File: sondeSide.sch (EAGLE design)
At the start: 33 parts

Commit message: I think its done, just needs labels
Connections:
- net 3.3V: now also JP15.1
- net 5V: no longer U$1.UGND1, U$1.UGND2
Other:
- moved on the sheet: JP25
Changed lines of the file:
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@@
 <sheet>
 <plain>
-<text x="-17.78" y="50.8" size="1.778" layer="91">Teensy VIN is on other side</text>
+<text x="12.7" y="50.8" size="1.778" layer="91">Teensy VIN is on other side</text>
 </plain>
 <instances>
@@
 <instance part="JP23" gate="G$1" x="-60.96" y="0" rot="R180"/>
 <instance part="JP24" gate="G$1" x="-60.96" y="-2.54" rot="R180"/>
-<instance part="JP25" gate="G$1" x="-5.08" y="55.88"/>
-<instance part="U$1" gate="G$1" x="-10.16" y="25.4"/>
+<instance part="JP25" gate="G$1" x="25.4" y="55.88"/>
+<instance part="U$1" gate="G$1" x="-10.16" y="43.18"/>
 </instances>
 <busses>
@@
 <wire x1="66.04" y1="12.7" x2="60.96" y2="12.7" width="0.1524" layer="91"/>
 <label x="60.96" y="12.7" size="1.778" layer="95" rot="R180"/>
+</segment>
+<segment>
+<pinref part="JP15" gate="G$1" pin="1"/>
+<wire x1="-58.42" y1="20.32" x2="-33.02" y2="20.32" width="0.1524" layer="91"/>
+<label x="-38.1" y="20.32" size="1.778" layer="95" rot="R180"/>
 </segment>
 </net>
@@
 <segment>
 <pinref part="JP25" gate="G$1" pin="1"/>
-<wire x1="-7.62" y1="55.88" x2="-12.7" y2="55.88" width="0.1524" layer="91"/>
-<label x="-15.24" y="55.88" size="1.778" layer="95" rot="R180"/>
-<pinref part="U$1" gate="G$1" pin="UGND1"/>
-<pinref part="U$1" gate="G$1" pin="UGND2"/>
-<wire x1="-12.7" y1="55.88" x2="-15.24" y2="55.88" width="0.1524" layer="91"/>
-<junction x="-12.7" y="55.88"/>
-</segment>
-</net>
+<wire x1="22.86" y1="55.88" x2="15.24" y2="55.88" width="0.1524" layer="91"/>
+<label x="15.24" y="55.88" size="1.778" layer="95" rot="R180"/>
+</segment>
+</net>

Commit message: I think its done
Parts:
- renumbered JP25 to VIN
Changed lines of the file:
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@@
 <part name="JP23" library="pinhead" library_urn="urn:adsk.eagle:library:325" deviceset="PINHD-1X1" device="" package3d_urn="urn:adsk.eagle:package:22485/2"/>
 <part name="JP24" library="pinhead" library_urn="urn:adsk.eagle:library:325" deviceset="PINHD-1X1" device="" package3d_urn="urn:adsk.eagle:package:22485/2"/>
-<part name="JP25" library="pinhead" library_urn="urn:adsk.eagle:library:325" deviceset="PINHD-1X1" device="" package3d_urn="urn:adsk.eagle:package:22485/2"/>
+<part name="VIN" library="pinhead" library_urn="urn:adsk.eagle:library:325" deviceset="PINHD-1X1" device="" package3d_urn="urn:adsk.eagle:package:22485/2"/>
 <part name="U$1" library="Teensy356" deviceset="TEENSY_3.5/3.6" device=""/>
 </parts>
@@
 <instance part="JP23" gate="G$1" x="-60.96" y="0" rot="R180"/>
 <instance part="JP24" gate="G$1" x="-60.96" y="-2.54" rot="R180"/>
-<instance part="JP25" gate="G$1" x="25.4" y="55.88"/>
+<instance part="VIN" gate="G$1" x="25.4" y="55.88"/>
 <instance part="U$1" gate="G$1" x="-10.16" y="43.18"/>
 </instances>
@@
 </segment>
 <segment>
-<pinref part="JP25" gate="G$1" pin="1"/>
+<pinref part="VIN" gate="G$1" pin="1"/>
 <wire x1="22.86" y1="55.88" x2="15.24" y2="55.88" width="0.1524" layer="91"/>
 <label x="15.24" y="55.88" size="1.778" layer="95" rot="R180"/>

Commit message: Without external 3.3v step down
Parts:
- removed U$1: TEENSY_3.5/3.6, Teensy356:TEENSY_3.5/3.6
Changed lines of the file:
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@@
 <part name="JP24" library="pinhead" library_urn="urn:adsk.eagle:library:325" deviceset="PINHD-1X1" device="" package3d_urn="urn:adsk.eagle:package:22485/2"/>
 <part name="VIN" library="pinhead" library_urn="urn:adsk.eagle:library:325" deviceset="PINHD-1X1" device="" package3d_urn="urn:adsk.eagle:package:22485/2"/>
-<part name="U$1" library="Teensy356" deviceset="TEENSY_3.5/3.6" device=""/>
 </parts>
 <sheets>
@@
 <instance part="JP24" gate="G$1" x="-60.96" y="-2.54" rot="R180"/>
 <instance part="VIN" gate="G$1" x="25.4" y="55.88"/>
-<instance part="U$1" gate="G$1" x="-10.16" y="43.18"/>
 </instances>
 <busses>
@@
 </drawing>
 <compatibility>
-<note version="6.3" minversion="6.2.2" severity="warning">
-Since Version 6.2.2 text objects can contain more than one line,
-which will not be processed correctly with this version.
-</note>
 <note version="8.2" severity="warning">
 Since Version 8.2, EAGLE supports online libraries. The ids

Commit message: Pre-routing
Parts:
- removed VIN: (no value), pinhead:PINHD-1X1
- added STEP-DOWN: 22-23-2041, con-molex:22-23-2041
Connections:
- net 3.3V: now also STEP-DOWN-1.S
- net 5V: now also STEP-DOWN-3.S; no longer VIN.1
- net GND: now also STEP-DOWN-2.S
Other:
- note removed: "Teensy VIN is on other side"
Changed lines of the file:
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@@
 <part name="JP23" library="pinhead" library_urn="urn:adsk.eagle:library:325" deviceset="PINHD-1X1" device="" package3d_urn="urn:adsk.eagle:package:22485/2"/>
 <part name="JP24" library="pinhead" library_urn="urn:adsk.eagle:library:325" deviceset="PINHD-1X1" device="" package3d_urn="urn:adsk.eagle:package:22485/2"/>
-<part name="VIN" library="pinhead" library_urn="urn:adsk.eagle:library:325" deviceset="PINHD-1X1" device="" package3d_urn="urn:adsk.eagle:package:22485/2"/>
+<part name="STEP-DOWN" library="con-molex" library_urn="urn:adsk.eagle:library:165" deviceset="22-23-2041" device=""/>
 </parts>
 <sheets>
 <sheet>
 <plain>
-<text x="12.7" y="50.8" size="1.778" layer="91">Teensy VIN is on other side</text>
 </plain>
 <instances>
@@
 <instance part="JP23" gate="G$1" x="-60.96" y="0" rot="R180"/>
 <instance part="JP24" gate="G$1" x="-60.96" y="-2.54" rot="R180"/>
-<instance part="VIN" gate="G$1" x="25.4" y="55.88"/>
+<instance part="STEP-DOWN" gate="-1" x="68.58" y="53.34"/>
+<instance part="STEP-DOWN" gate="-2" x="68.58" y="50.8"/>
+<instance part="STEP-DOWN" gate="-3" x="68.58" y="48.26"/>
+<instance part="STEP-DOWN" gate="-4" x="68.58" y="45.72"/>
 </instances>
 <busses>
@@
 <wire x1="-58.42" y1="20.32" x2="-33.02" y2="20.32" width="0.1524" layer="91"/>
 <label x="-38.1" y="20.32" size="1.778" layer="95" rot="R180"/>
+</segment>
+<segment>
+<pinref part="STEP-DOWN" gate="-1" pin="S"/>
+<wire x1="66.04" y1="53.34" x2="60.96" y2="53.34" width="0.1524" layer="91"/>
+<label x="60.96" y="53.34" size="1.778" layer="95" rot="R180"/>
 </segment>
 </net>
@@
 <wire x1="60.96" y1="5.08" x2="66.04" y2="5.08" width="0.1524" layer="91"/>
 <label x="60.96" y="5.08" size="1.778" layer="95" rot="R180"/>
+</segment>
+<segment>
+<pinref part="STEP-DOWN" gate="-2" pin="S"/>
+<wire x1="60.96" y1="50.8" x2="66.04" y2="50.8" width="0.1524" layer="91"/>
+<label x="60.96" y="50.8" size="1.778" layer="95" rot="R180"/>
 </segment>
 </net>
@@
 </segment>
 <segment>
-<pinref part="VIN" gate="G$1" pin="1"/>
-<wire x1="22.86" y1="55.88" x2="15.24" y2="55.88" width="0.1524" layer="91"/>
-<label x="15.24" y="55.88" size="1.778" layer="95" rot="R180"/>
-</segment>
-</net>
+<pinref part="STEP-DOWN" gate="-3" pin="S"/>
+<wire x1="66.04" y1="48.26" x2="60.96" y2="48.26" width="0.1524" layer="91"/>
+<label x="60.96" y="48.26" size="1.778" layer="95" rot="R180"/>
+</segment>
+</net>

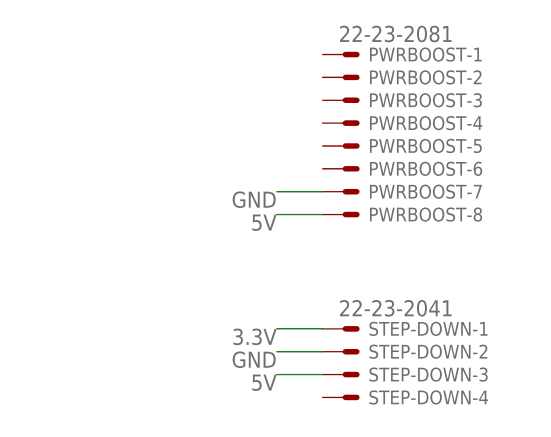
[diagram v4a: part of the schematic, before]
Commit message: Everything but ground plane
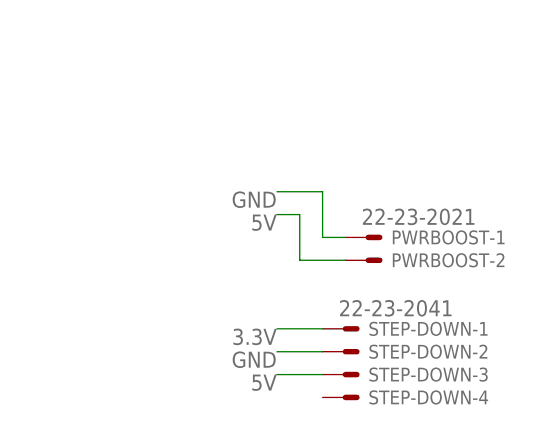
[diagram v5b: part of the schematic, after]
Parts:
- PWRBOOST: value 22-23-2081 -> 22-23-2021; device con-molex:22-23-2081 -> con-molex:22-23-2021; SPICEPREFIX X -> (none)
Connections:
- net 5V: now also PWRBOOST-2.S; no longer PWRBOOST-8.S
- net GND: now also PWRBOOST-1.S; no longer PWRBOOST-7.S
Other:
- moved on the sheet: PWRBOOST-1, PWRBOOST-2
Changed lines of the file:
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@@
 <layer number="2" name="Route2" color="1" fill="3" visible="no" active="no"/>
 <layer number="3" name="Route3" color="4" fill="3" visible="no" active="no"/>
+<layer number="4" name="Route4" color="1" fill="4" visible="no" active="no"/>
+<layer number="5" name="Route5" color="4" fill="4" visible="no" active="no"/>
+<layer number="6" name="Route6" color="1" fill="8" visible="no" active="no"/>
+<layer number="7" name="Route7" color="4" fill="8" visible="no" active="no"/>
+<layer number="8" name="Route8" color="1" fill="2" visible="no" active="no"/>
+<layer number="9" name="Route9" color="4" fill="2" visible="no" active="no"/>
+<layer number="10" name="Route10" color="1" fill="7" visible="no" active="no"/>
+<layer number="11" name="Route11" color="4" fill="7" visible="no" active="no"/>
+<layer number="12" name="Route12" color="1" fill="5" visible="no" active="no"/>
+<layer number="13" name="Route13" color="4" fill="5" visible="no" active="no"/>
 <layer number="14" name="Route14" color="1" fill="6" visible="no" active="no"/>
 <layer number="15" name="Route15" color="4" fill="6" visible="no" active="no"/>
@@
 </classes>
 <parts>
-<part name="PWRBOOST" library="con-molex" library_urn="urn:adsk.eagle:library:165" deviceset="22-23-2081" device="">
-<attribute name="SPICEPREFIX" value="X"/>
-</part>
 <part name="STEP-UP" library="con-molex" library_urn="urn:adsk.eagle:library:165" deviceset="22-23-2031" device=""/>
 <part name="SONDE" library="con-molex" library_urn="urn:adsk.eagle:library:165" deviceset="22-23-2051" device=""/>
@@
 <part name="JP24" library="pinhead" library_urn="urn:adsk.eagle:library:325" deviceset="PINHD-1X1" device="" package3d_urn="urn:adsk.eagle:package:22485/2"/>
 <part name="STEP-DOWN" library="con-molex" library_urn="urn:adsk.eagle:library:165" deviceset="22-23-2041" device=""/>
+<part name="PWRBOOST" library="con-molex" library_urn="urn:adsk.eagle:library:165" deviceset="22-23-2021" device=""/>
 </parts>
 <sheets>
@@
 </plain>
 <instances>
-<instance part="PWRBOOST" gate="-1" x="68.58" y="83.82"/>
-<instance part="PWRBOOST" gate="-2" x="68.58" y="81.28"/>
-<instance part="PWRBOOST" gate="-3" x="68.58" y="78.74"/>
-<instance part="PWRBOOST" gate="-4" x="68.58" y="76.2"/>
-<instance part="PWRBOOST" gate="-5" x="68.58" y="73.66"/>
-<instance part="PWRBOOST" gate="-6" x="68.58" y="71.12"/>
-<instance part="PWRBOOST" gate="-7" x="68.58" y="68.58"/>
-<instance part="PWRBOOST" gate="-8" x="68.58" y="66.04"/>
 <instance part="STEP-UP" gate="-1" x="68.58" y="30.48"/>
 <instance part="STEP-UP" gate="-2" x="68.58" y="27.94"/>
@@
 <instance part="STEP-DOWN" gate="-3" x="68.58" y="48.26"/>
 <instance part="STEP-DOWN" gate="-4" x="68.58" y="45.72"/>
+<instance part="PWRBOOST" gate="-1" x="71.12" y="63.5"/>
+<instance part="PWRBOOST" gate="-2" x="71.12" y="60.96"/>
 </instances>
 <busses>
@@
 </segment>
 <segment>
-<pinref part="PWRBOOST" gate="-7" pin="S"/>
 <wire x1="66.04" y1="68.58" x2="60.96" y2="68.58" width="0.1524" layer="91"/>
 <label x="60.96" y="68.58" size="1.778" layer="95" rot="R180"/>
+<pinref part="PWRBOOST" gate="-1" pin="S"/>
+<wire x1="68.58" y1="63.5" x2="66.04" y2="63.5" width="0.1524" layer="91"/>
+<wire x1="66.04" y1="63.5" x2="66.04" y2="68.58" width="0.1524" layer="91"/>
 </segment>
 <segment>
@@
 <net name="5V" class="0">
 <segment>
-<pinref part="PWRBOOST" gate="-8" pin="S"/>
-<wire x1="60.96" y1="66.04" x2="66.04" y2="66.04" width="0.1524" layer="91"/>
+<wire x1="60.96" y1="66.04" x2="63.5" y2="66.04" width="0.1524" layer="91"/>
 <label x="60.96" y="66.04" size="1.778" layer="95" rot="R180"/>
-</segment>
-<segment>
+<pinref part="PWRBOOST" gate="-2" pin="S"/>
+<wire x1="63.5" y1="66.04" x2="63.5" y2="60.96" width="0.1524" layer="91"/>
+<wire x1="63.5" y1="60.96" x2="68.58" y2="60.96" width="0.1524" layer="91"/>
+</segment>
+<segment>

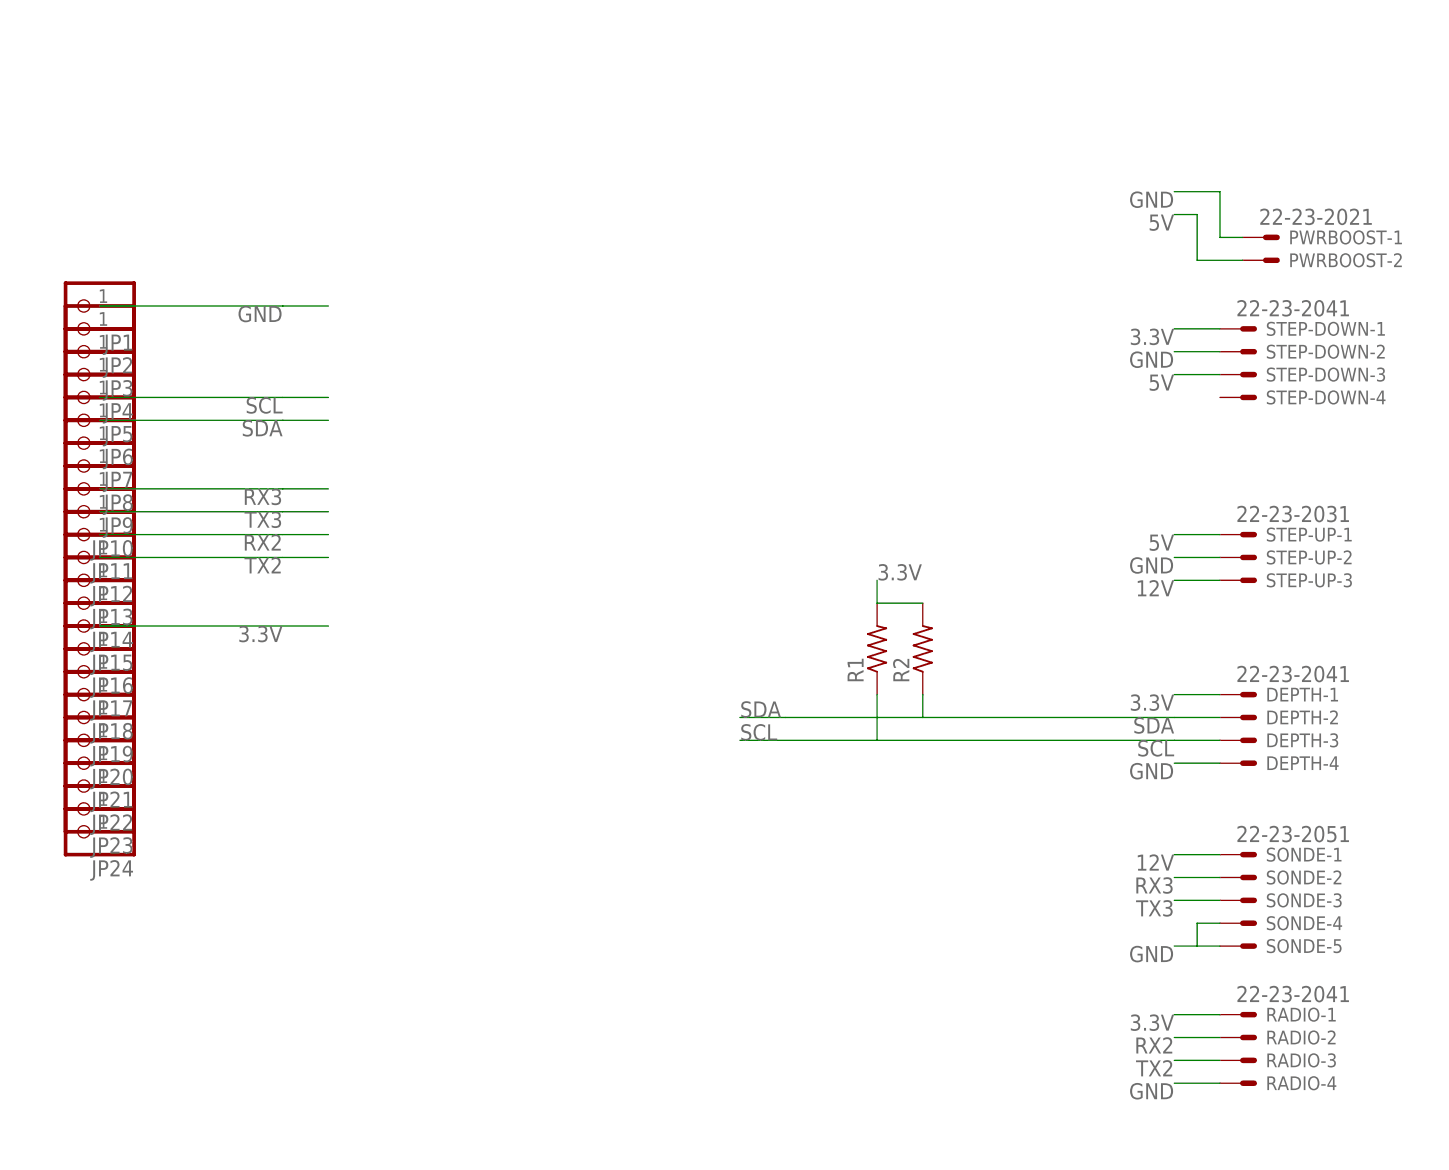
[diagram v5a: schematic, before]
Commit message: Proposed layout, routing time
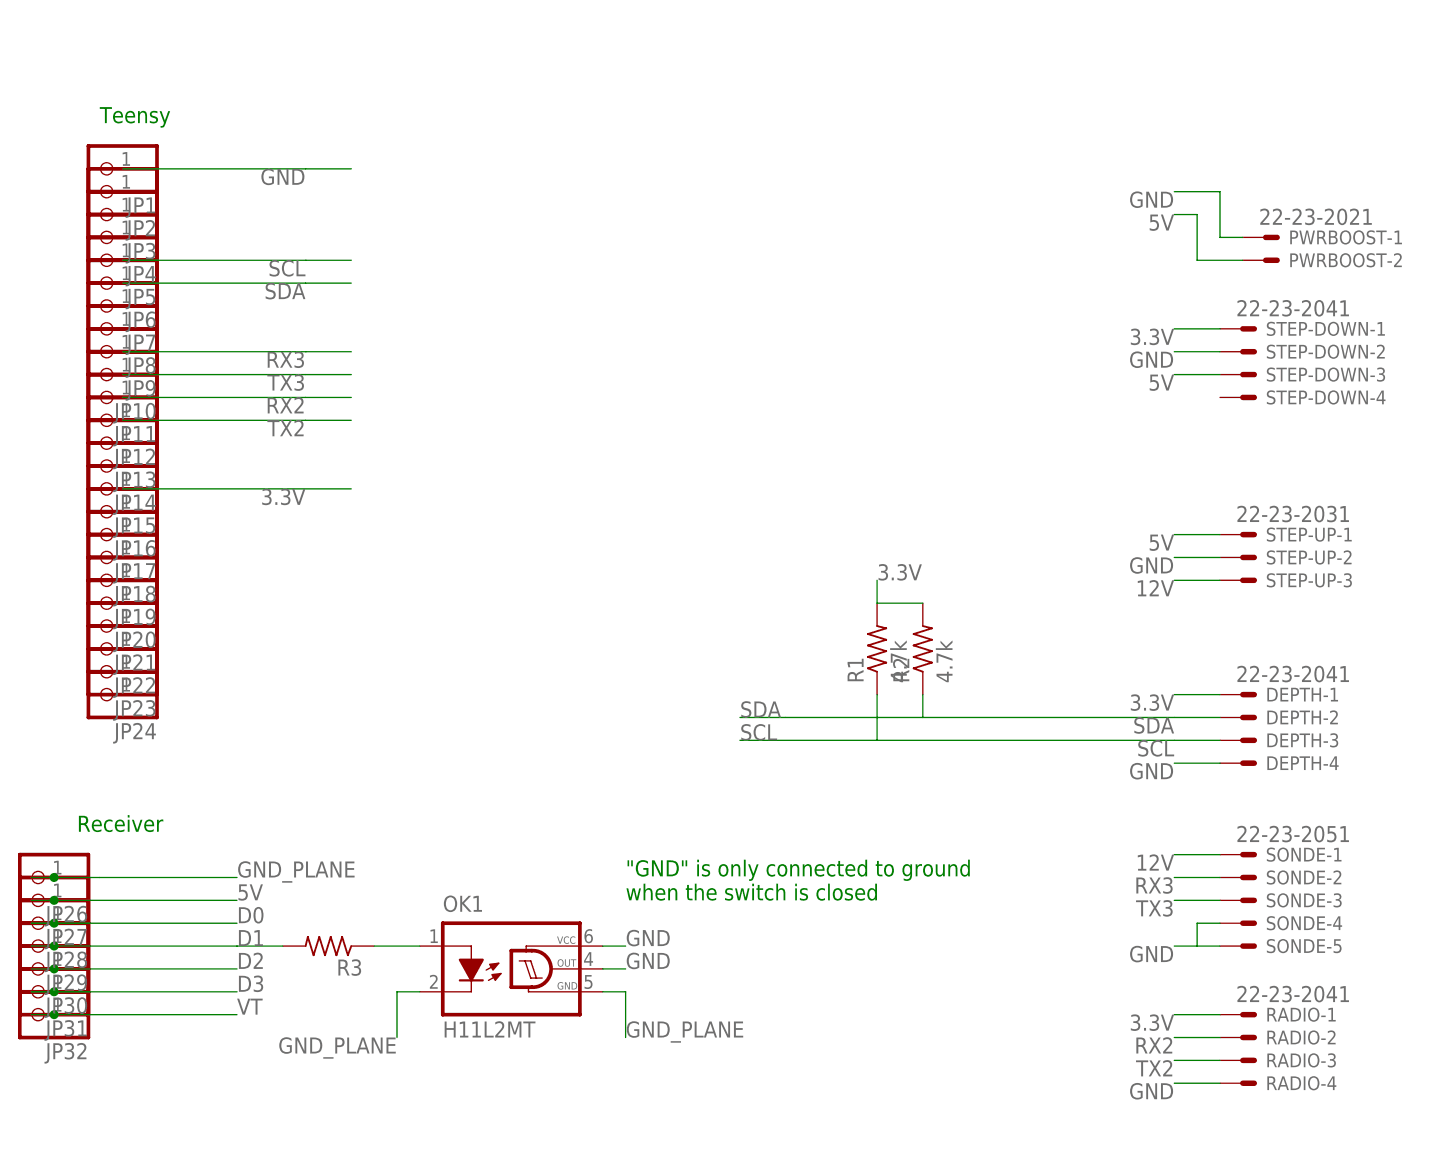
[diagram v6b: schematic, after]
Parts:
- added JP26, JP27, JP28, JP29, JP30, JP31, JP32: (no value), pinhead:PINHD-1X1
- added OK1: H11L2MT, optocoupler:H11L2MT
- added R3: (no value), rcl:R-US_0204/7
- R1, R2: value (none) -> 4.7k
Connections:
- new net D0: JP28.1
- new net D1: JP29.1, R3.2
- new net D2: JP30.1
- new net D3: JP31.1
- new net GND_PLANE: JP26.1, OK1.C, OK1.GND
- new net N$1: OK1.A, R3.1
- new net VT: JP32.1
- net 5V: now also JP27.1
- net GND: now also OK1.OUT, OK1.VCC
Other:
- note added: ""GND" is only connected to ground when the switch is closed"
- note added: "Receiver"
- note added: "Teensy"
- moved on the sheet: JP1, JP10, JP11, JP12, JP13, JP14, JP15, JP16, JP17, JP18, JP19, JP2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

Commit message: About to do significant rerouting
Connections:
- net GND: no longer PWRBOOST-1.S
- net GND_PLANE: now also PWRBOOST-1.S
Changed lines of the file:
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@@
-</segment>
-<segment>
-<wire x1="66.04" y1="68.58" x2="60.96" y2="68.58" width="0.1524" layer="91"/>
-<label x="60.96" y="68.58" size="1.778" layer="95" rot="R180"/>
-<pinref part="PWRBOOST" gate="-1" pin="S"/>
-<wire x1="68.58" y1="63.5" x2="66.04" y2="63.5" width="0.1524" layer="91"/>
-<wire x1="66.04" y1="63.5" x2="66.04" y2="68.58" width="0.1524" layer="91"/>
 </segment>
 <segment>
@@
 <pinref part="OK1" gate="G$1" pin="A"/>
 <wire x1="-27.94" y1="-15.24" x2="-22.86" y2="-15.24" width="0.1524" layer="91"/>
+<junction x="-22.86" y="-15.24"/>
 </segment>
 </net>
@@
 <label x="0" y="-25.4" size="1.778" layer="95"/>
 </segment>
-</net>
+<segment>
+<wire x1="66.04" y1="68.58" x2="60.96" y2="68.58" width="0.1524" layer="91"/>
+<label x="60.96" y="68.58" size="1.778" layer="95" rot="R180"/>
+<pinref part="PWRBOOST" gate="-1" pin="S"/>
+<wire x1="68.58" y1="63.5" x2="66.04" y2="63.5" width="0.1524" layer="91"/>
+<wire x1="66.04" y1="63.5" x2="66.04" y2="68.58" width="0.1524" layer="91"/>
+</segment>
+</net>
